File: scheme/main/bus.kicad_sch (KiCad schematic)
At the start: 12 parts, among them SW1 CAN_TERM, U21 SN65HVD233

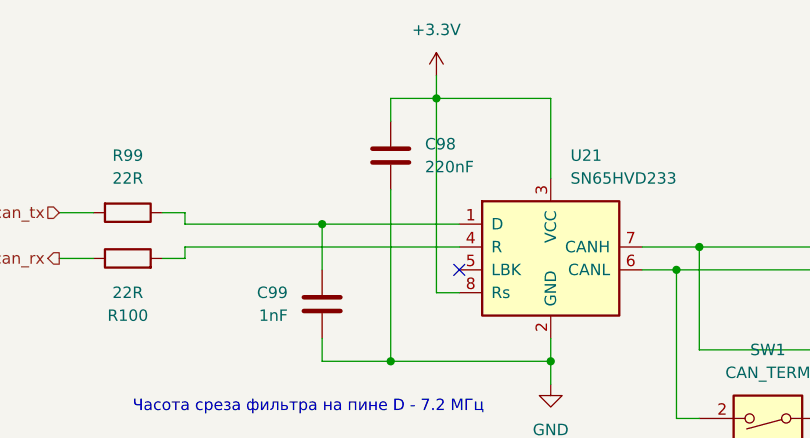
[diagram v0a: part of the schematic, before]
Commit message: replace some 220n capacitors with 100n
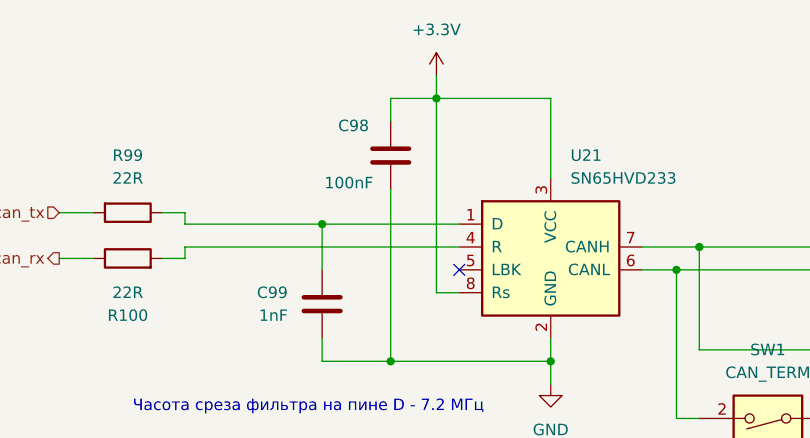
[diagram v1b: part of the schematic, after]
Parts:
- C98: value 220nF -> 100nF
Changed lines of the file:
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@@
 		(on_board yes)
 		(dnp no)
-		(fields_autoplaced yes)
 		(property "Reference" "C98"
-			(at 110.49 72.3899 0)
+			(at 100.838 70.358 0)
 			(effects
 				(font
@@
 			)
 		)
-		(property "Value" "220nF"
-			(at 110.49 74.9299 0)
+		(property "Value" "100nF"
+			(at 99.314 76.708 0)
 			(effects
 				(font

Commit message: sheets titles
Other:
- note added: "CAN"
- title: (none) -> Цифровые шины
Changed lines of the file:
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@@
 	(generator_version "8.0")
 	(paper "A4")
+	(title_block
+		(title "Цифровые шины")
+	)
 	(junction
 		(at 138.43 86.36)
@@
 		)
 	)
+	(text "CAN"
+		(exclude_from_sim no)
+		(at 122.936 61.976 0)
+		(effects
+			(font
+				(size 2.54 2.54)
+			)
+			(justify left)
+		)
+	)

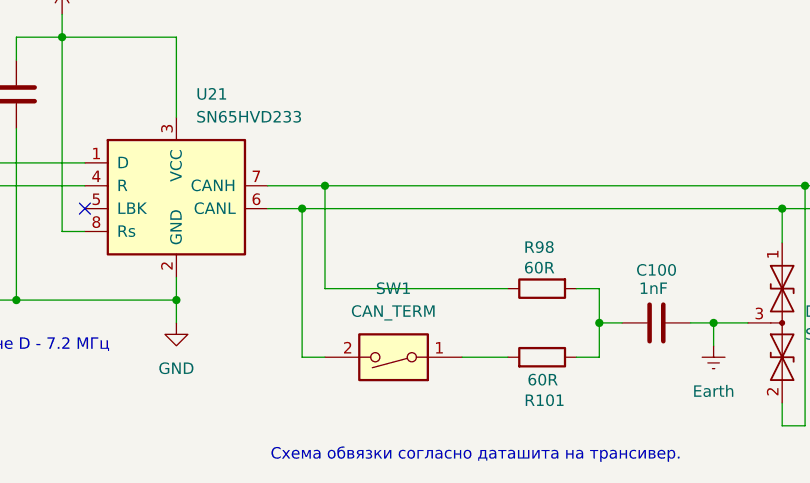
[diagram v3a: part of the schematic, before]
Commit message: can bus terminator dip1 replaced with dip2
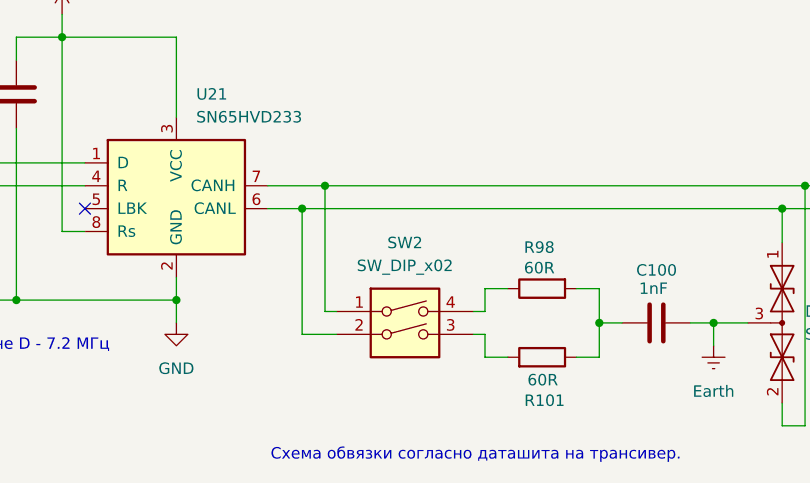
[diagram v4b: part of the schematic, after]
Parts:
- removed SW1: CAN_TERM, symbol Switch:SW_DIP_x01
- added SW2: SW_DIP_x02, symbol Switch:SW_DIP_x02
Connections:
- net can_hi: now also SW2.1; no longer R98.1
- net can_lo: now also SW2.2
- net at R101.2: now also SW2.3
- new net: R98.1, SW2.4
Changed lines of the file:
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@@
 	(wire
 		(pts
-			(xy 138.43 86.36) (xy 138.43 102.87)
+			(xy 138.43 86.36) (xy 138.43 100.33)
+		)
+		(stroke
+			(width 0)
+			(type default)
+		)
+	)
+	(wire
+		(pts
+			(xy 158.75 97.79) (xy 158.75 95.25)
 		)
 		(stroke
@@
 	(wire
 		(pts
+			(xy 158.75 95.25) (xy 161.29 95.25)
+		)
+		(stroke
+			(width 0)
+			(type default)
+		)
+	)
+	(wire
+		(pts
 			(xy 69.85 85.09) (xy 73.66 85.09)
 		)
@@
 	(wire
 		(pts
+			(xy 157.48 100.33) (xy 158.75 100.33)
+		)
+		(stroke
+			(width 0)
+			(type default)
+		)
+	)
+	(wire
+		(pts
 			(xy 222.25 83.82) (xy 232.41 83.82)
 		)
@@
 	(wire
 		(pts
-			(xy 156.21 102.87) (xy 161.29 102.87)
+			(xy 158.75 100.33) (xy 158.75 102.87)
 		)
 		(stroke
@@
 	(wire
 		(pts
-			(xy 140.97 102.87) (xy 138.43 102.87)
+			(xy 138.43 100.33) (xy 142.24 100.33)
 		)
 		(stroke
@@
 	(wire
 		(pts
-			(xy 161.29 95.25) (xy 140.97 95.25)
-		)
-		(stroke
-			(width 0)
-			(type default)
-		)
-	)
-	(wire
-		(pts
 			(xy 106.68 67.31) (xy 106.68 69.85)
 		)
@@
 	(wire
 		(pts
-			(xy 140.97 95.25) (xy 140.97 83.82)
+			(xy 140.97 83.82) (xy 140.97 97.79)
 		)
 		(stroke
@@
 	(wire
 		(pts
+			(xy 140.97 97.79) (xy 142.24 97.79)
+		)
+		(stroke
+			(width 0)
+			(type default)
+		)
+	)
+	(wire
+		(pts
 			(xy 171.45 102.87) (xy 168.91 102.87)
 		)
@@
 	(wire
 		(pts
+			(xy 157.48 97.79) (xy 158.75 97.79)
+		)
+		(stroke
+			(width 0)
+			(type default)
+		)
+	)
+	(wire
+		(pts
 			(xy 184.15 99.06) (xy 187.96 99.06)
+		)
+		(stroke
+			(width 0)
+			(type default)
+		)
+	)
+	(wire
+		(pts
+			(xy 158.75 102.87) (xy 161.29 102.87)
 		)
 		(stroke
@@
 	)
 	(symbol
-		(lib_id "Switch:SW_DIP_x01")
-		(at 148.59 102.87 180)
-		(unit 1)
-		(exclude_from_sim no)
-		(in_bom yes)
-		(on_board yes)
-		(dnp no)
-		(fields_autoplaced yes)
-		(property "Reference" "SW1"
-			(at 148.59 95.25 0)
-			(effects
-				(font
-					(size 1.27 1.27)
-				)
-			)
-		)
-		(property "Value" "CAN_TERM"
-			(at 148.59 97.79 0)
-			(effects
-				(font
-					(size 1.27 1.27)
-				)
-			)
-		)
-		(property "Footprint" ""
-			(at 148.59 102.87 0)
-			(effects
-				(font
-					(size 1.27 1.27)
-				)
-				(hide yes)
-			)
-		)
-		(property "Datasheet" "~"
-			(at 148.59 102.87 0)
-			(effects
-				(font
-					(size 1.27 1.27)
-				)
-				(hide yes)
-			)
-		)
-		(property "Description" "1x DIP Switch, Single Pole Single Throw (SPST) switch, small symbol"
-			(at 148.59 102.87 0)
-			(effects
-				(font
-					(size 1.27 1.27)
-				)
-				(hide yes)
-			)
-		)
-		(pin "2"
-		)
-		(pin "1"
-		)
-		(instances
-			(project ""
-				(path "/c11d1dbc-4db9-4712-8d1d-5f6f7086cded/dd58f61f-c5ca-456a-ab08-38b10841227b"
-					(reference "SW1")
-					(unit 1)
-				)
-			)
-		)
-	)
-	(symbol
 		(lib_id "Device:C")
 		(at 222.25 92.71 0)
@@
 					(unit 1)
 				)
+			)
+		)
+	)
+	(symbol
+		(lib_id "Switch:SW_DIP_x02")
+		(at 149.86 100.33 0)
+		(unit 1)
+		(exclude_from_sim no)
+		(in_bom yes)
+		(on_board yes)
+		(dnp no)
+		(property "Reference" "SW2"
+			(at 149.86 90.17 0)
+			(effects
+				(font
+					(size 1.27 1.27)
+				)
+			)
+		)
+		(property "Value" "SW_DIP_x02"
+			(at 149.86 92.71 0)
+			(effects
+				(font
+					(size 1.27 1.27)
+				)
+			)
+		)
+		(property "Footprint" ""
+			(at 149.86 100.33 0)
+			(effects
+				(font
+					(size 1.27 1.27)
+				)
+				(hide yes)
+			)
+		)
+		(property "Datasheet" "~"
+			(at 149.86 100.33 0)
+			(effects
+				(font
+					(size 1.27 1.27)
+				)
+				(hide yes)
+			)
+		)
+		(property "Description" "2x DIP Switch, Single Pole Single Throw (SPST) switch, small symbol"
+			(at 149.86 100.33 0)
+			(effects
+				(font
+					(size 1.27 1.27)
+				)
+				(hide yes)
+			)
+		)
+		(pin "1"
+		)
+		(pin "2"
+		)
+		(pin "3"
+		)
+		(pin "4"
+		)
+		(instances
+			(project ""
+				(path "/c11d1dbc-4db9-4712-8d1d-5f6f7086cded/dd58f61f-c5ca-456a-ab08-38b10841227b"
+					(reference "SW2")
+					(unit 1)
+				)

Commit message: footprints set/changed
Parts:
- SW2: footprint (none) -> Button_Switch_THT:SW_DIP_SPSTx02_Slide_9.78x7.26mm_W7.62mm_P2.54mm
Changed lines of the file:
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@@
 			)
 		)
-		(property "Footprint" ""
+		(property "Footprint" "Button_Switch_THT:SW_DIP_SPSTx02_Slide_9.78x7.26mm_W7.62mm_P2.54mm"
 			(at 149.86 100.33 0)
 			(effects
